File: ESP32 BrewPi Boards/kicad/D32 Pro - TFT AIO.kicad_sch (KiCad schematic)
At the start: 33 parts, among them J1 POWER, J2 5V IN, J3 TFT, J4 RELAY, J5 LCD, J6 RJ45, J7 GLYCOL, J8 OW_VSEL, Q1 BSS123, Q2 BSS123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

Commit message: Fix footprint for U1
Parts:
- J3: LCSC (none) -> C5665
- J6: LCSC (none) -> C3000202
- U1: footprint PCM_Package_DIP_AKL:DIP-4_W7.62mm_SMDSocket_SmallPads -> PCM_Package_DIP_AKL:DIP-4_W8.89mm_SMDSocket_LongPads
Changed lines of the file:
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@@
       (effects (font (size 1.27 1.27)))
     )
-    (property "Footprint" "PCM_Package_DIP_AKL:DIP-4_W7.62mm_SMDSocket_SmallPads" (at 130.81 140.97 0)
+    (property "Footprint" "PCM_Package_DIP_AKL:DIP-4_W8.89mm_SMDSocket_LongPads" (at 130.81 140.97 0)
       (effects (font (size 1.27 1.27) italic) (justify left) hide)
     )
@@
       (effects (font (size 1.27 1.27)) hide)
     )
+    (property "LCSC" "C3000202" (at 60.96 96.52 0)
+      (effects (font (size 1.27 1.27)) hide)
+    )
     (pin "1")
     (pin "2")
@@
       (effects (font (size 1.27 1.27)) hide)
     )
+    (property "LCSC" "C5665" (at 99.06 36.83 0)
+      (effects (font (size 1.27 1.27)) hide)
+    )

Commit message: Add schematic note
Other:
- note added: "Either R1 (SMD) or R2 (TH) should be used"
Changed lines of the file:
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@@
+    (effects (font (size 1.27 1.27)) (justify left bottom))
+  )
+  (text "Either R1 (SMD) or R2 (TH) should be used" (at 73.66 99.06 0)
     (effects (font (size 1.27 1.27)) (justify left bottom))
   )

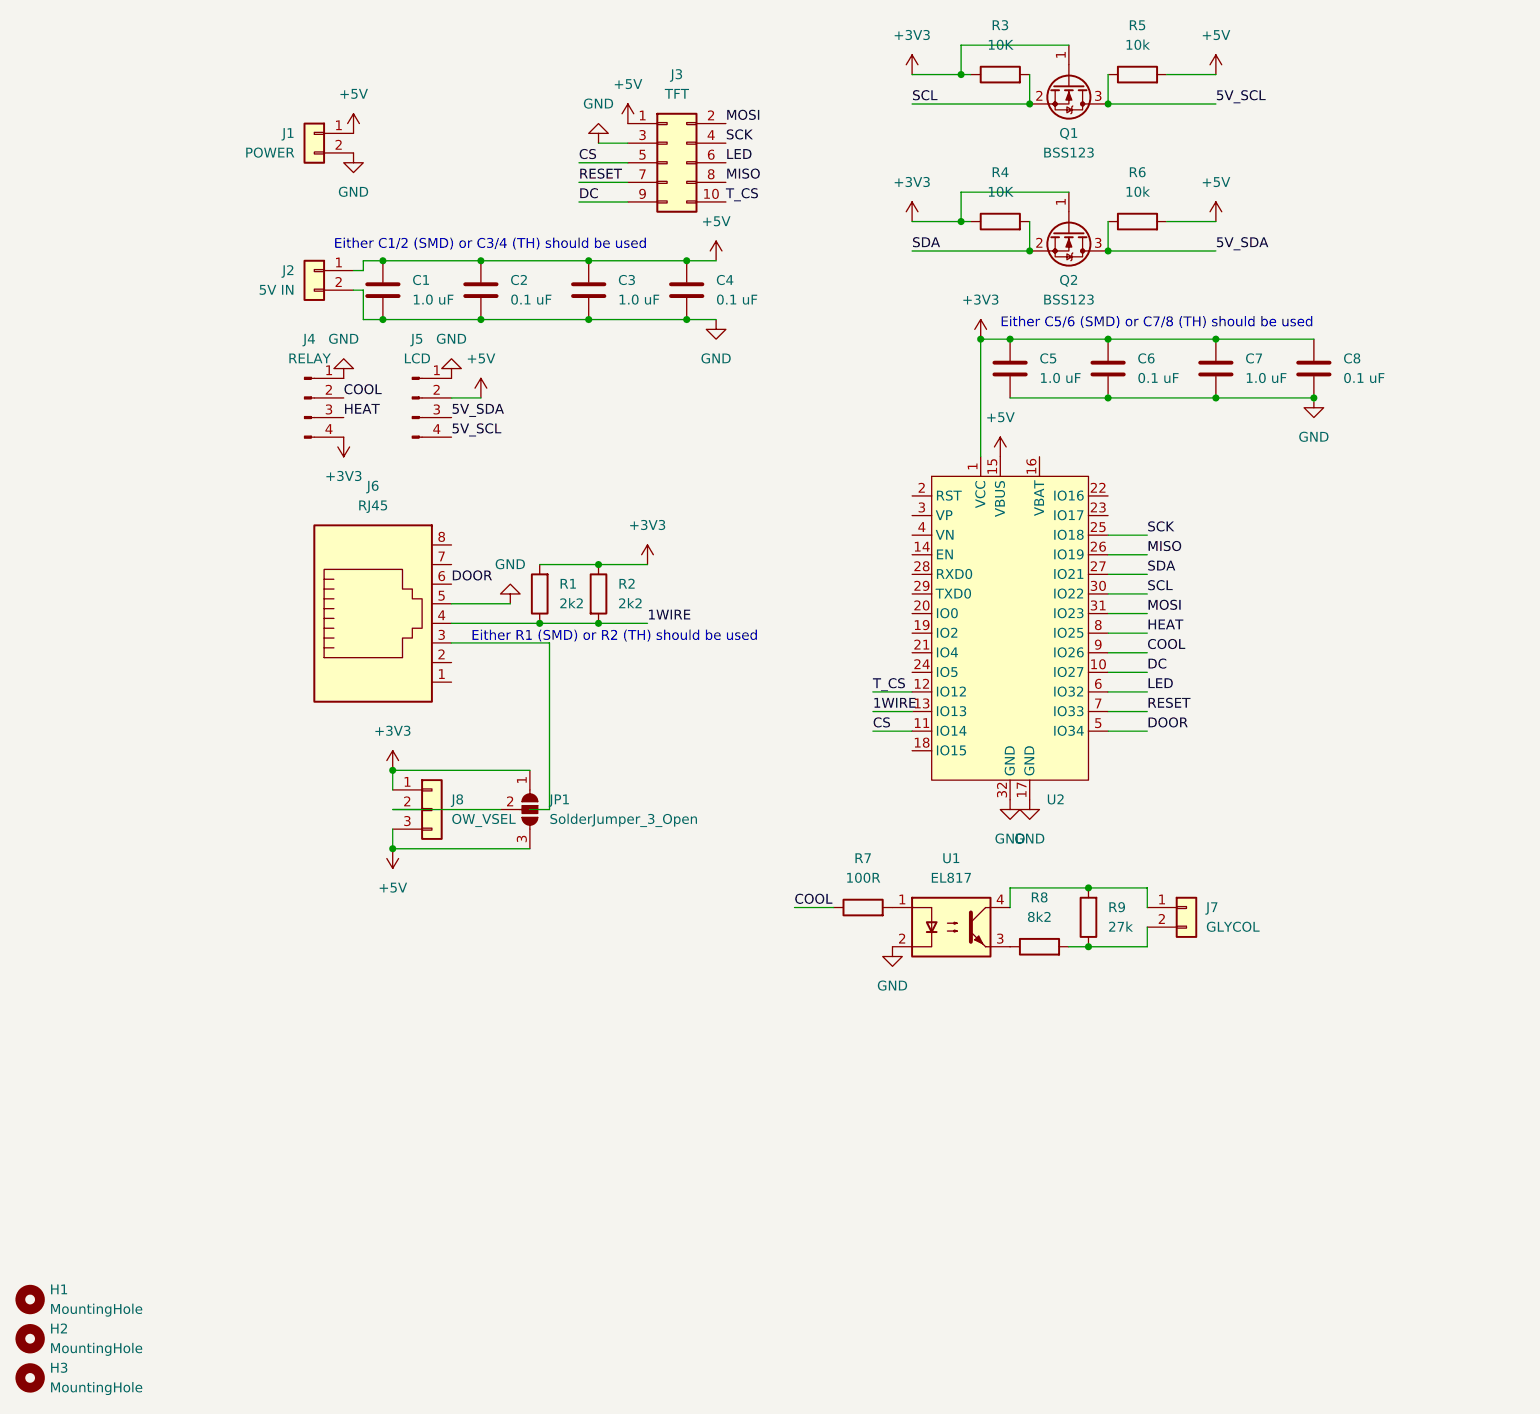
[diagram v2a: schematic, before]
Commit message: Power to OneWire sensors
Add trace for power to onewire sensors, adjust silkscreen
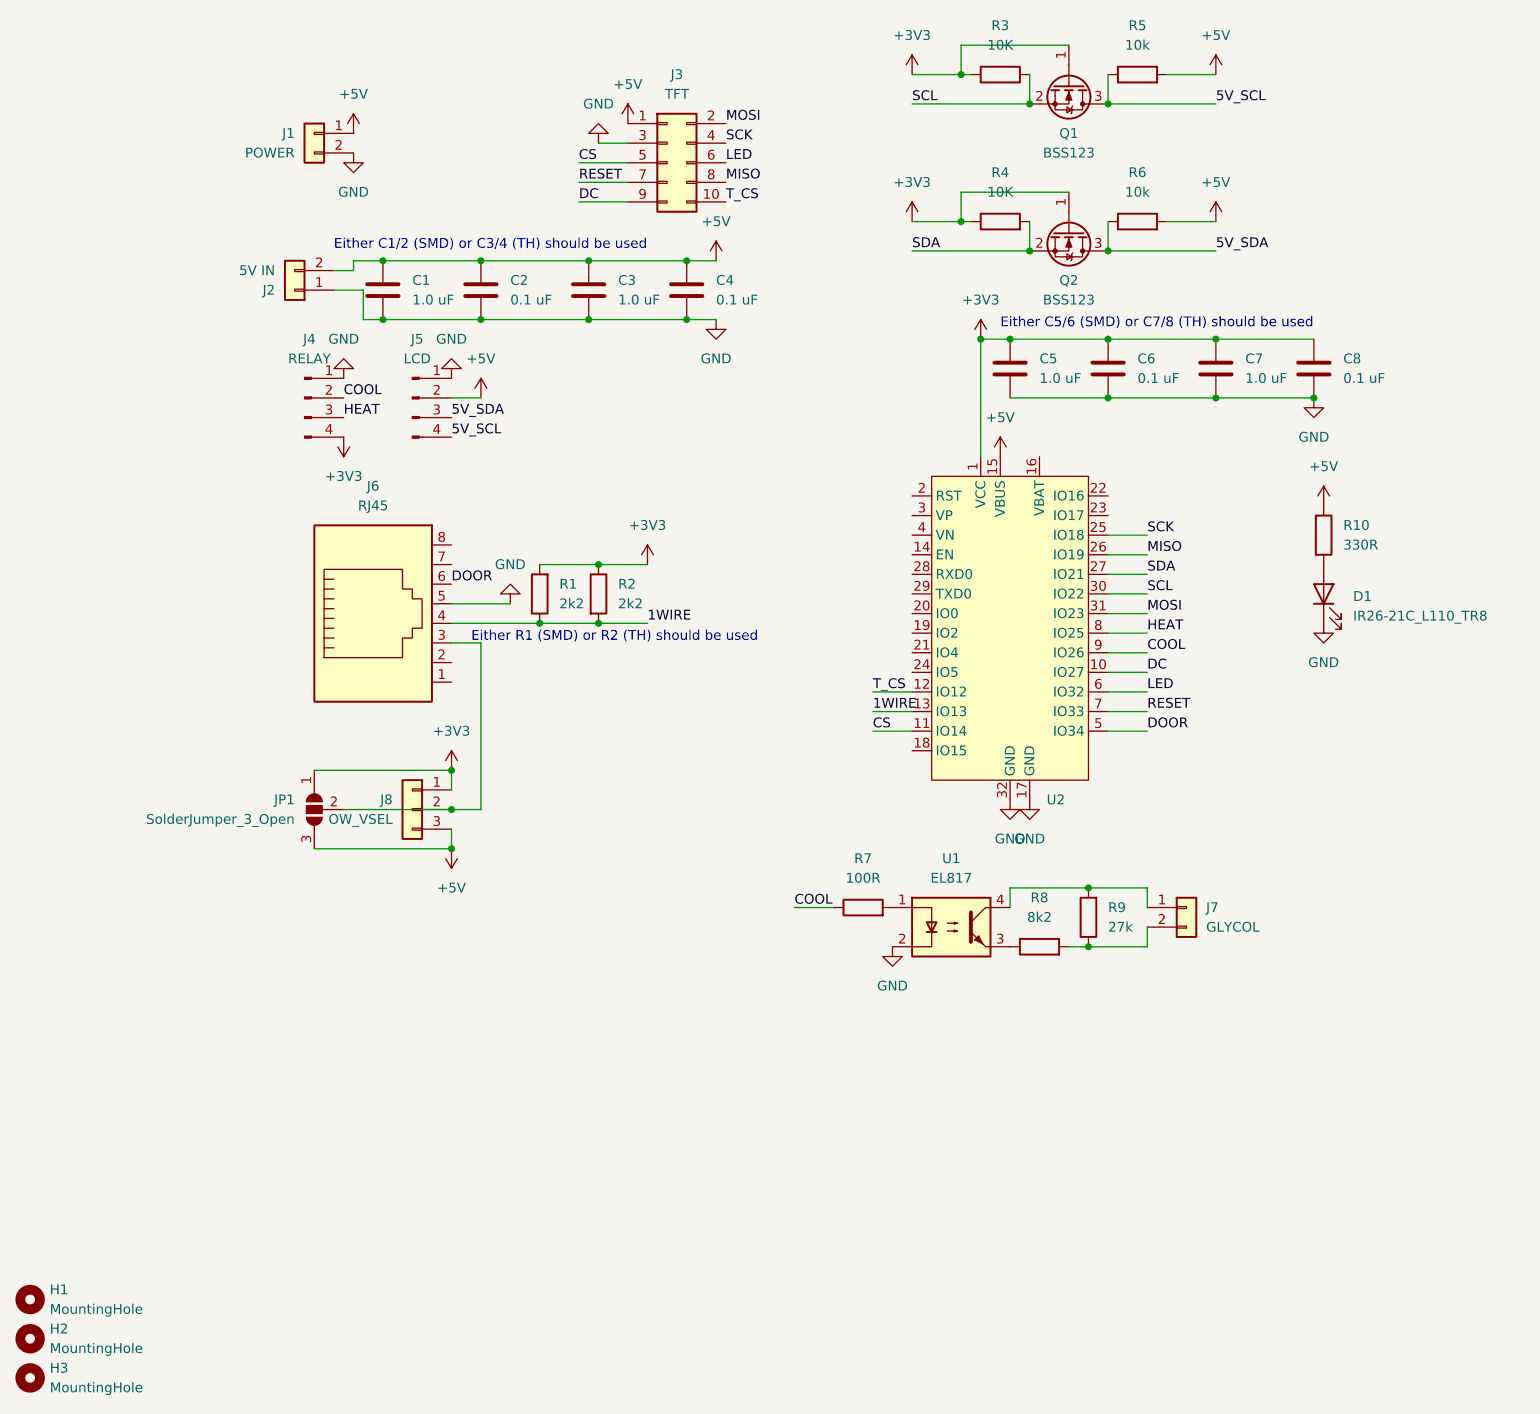
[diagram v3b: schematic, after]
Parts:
- added D1: IR26-21C_L110_TR8, LED_SMD:LED_0805_2012Metric_Pad1.15x1.40mm_HandSolder, symbol LED:IR26-21C_L110_TR8
- added R10: 330R, Resistor_SMD:R_0805_2012Metric_Pad1.20x1.40mm_HandSolder, symbol Device:R
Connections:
- net +5V: now also J2.2 (Pin_2), R10.1; no longer J2.1 (Pin_1)
- net GND: now also J2.1 (Pin_1), D1.1 (K); no longer J2.2 (Pin_2)
- net at J8.2 (Pin_2), JP1.2 (C): now also J6.3
- new net: D1.2 (A), R10.2
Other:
- moved on the sheet: J2, J8, JP1
